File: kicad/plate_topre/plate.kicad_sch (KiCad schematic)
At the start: 72 parts, among them SW1 SW_Push, SW10 SW_Push, SW11 SW_Push, SW12 SW_Push, SW13 SW_Push, SW14 SW_Push, SW15 SW_Push, SW16 SW_Push, SW17 SW_Push, SW18 SW_Push, SW19 SW_Push, SW2 SW_Push, SW20 SW_Push, SW21 SW_Push, SW22 SW_Push, SW23 SW_Push, SW24 SW_Push, SW25 SW_Push, SW26 SW_Push, SW27 SW_Push, SW28 SW_Push, SW29 SW_Push, SW3 SW_Push, SW30 SW_Push, SW31 SW_Push, SW32 SW_Push, SW33 SW_Push, SW34 SW_Push, SW35 SW_Push, SW36 SW_Push, SW37 SW_Push, SW38 SW_Push, SW39 SW_Push, SW4 SW_Push, SW40 SW_Push, SW41 SW_Push, SW42 SW_Push, SW43 SW_Push, SW44 SW_Push, SW45 SW_Push, SW5 SW_Push, SW6 SW_Push, SW7 SW_Push, SW8 SW_Push, SW9 SW_Push

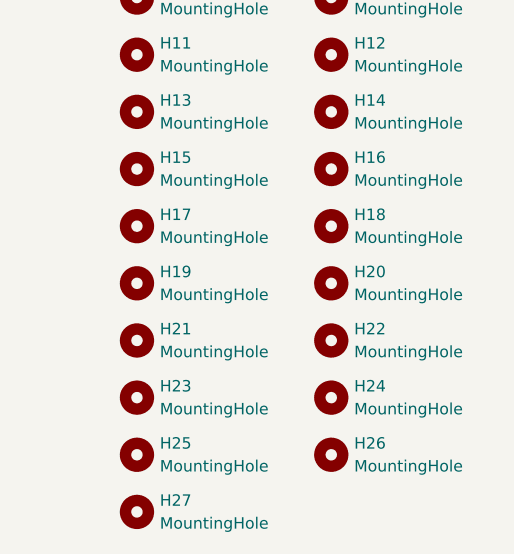
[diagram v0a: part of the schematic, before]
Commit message: updated footprint and fixing plate tolerance
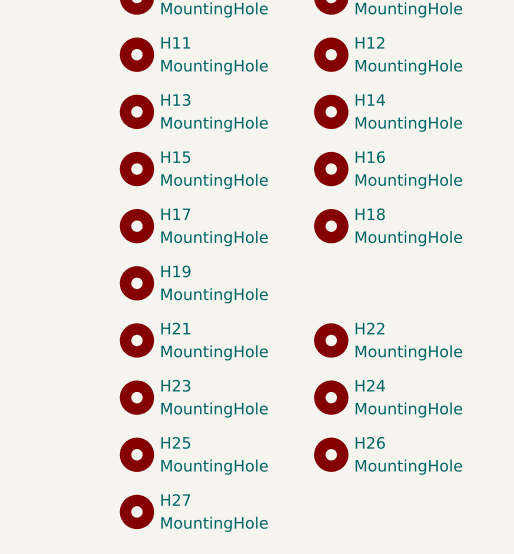
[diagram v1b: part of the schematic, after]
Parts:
- removed H20: MountingHole, MountingHole:MountingHole_3.2mm_M3_DIN965, symbol Mechanical:MountingHole
- H1, H10, H11, H12, H13, H14, H15, H16, H17, H18, H19, H2, H21, H22, H23, H24, H25, H26, H27, H3, H4, H5, H6, H7, H8, H9: footprint MountingHole:MountingHole_3.2mm_M3_DIN965 -> capacitive_sensors:MountingHole_2.2mm_M2
- SW1, SW10, SW11, SW12, SW13, SW15, SW16, SW17, SW18, SW19, SW2, SW20, SW21, SW22, SW23, SW24, SW25, SW27, SW28, SW29, SW3, SW30, SW31, SW32, SW33, SW34, SW35, SW36, SW37, SW4, SW5, SW6, SW7, SW8, SW9: footprint capacitive_sensors:ec_plate_cutout_topre_14.1x14.7mm -> capacitive_sensors:plate_cut_1U_topre
- SW14, SW39, SW44: footprint capacitive_sensors:ec_plate_cutout_topre_14.1x14.7mm -> capacitive_sensors:plate_cut_combo_0.25u_offset_topre
- SW26, SW41, SW42: footprint capacitive_sensors:ec_plate_cutout_topre_2u -> capacitive_sensors:plate_cut_2U_topre
- SW38, SW45: footprint capacitive_sensors:ec_plate_cutout_topre_14.1x14.7mm -> capacitive_sensors:plate_cut_combo_0.125u_offset_topre
- SW40, SW43: footprint capacitive_sensors:ec_plate_cutout_topre_14.1x14.7mm -> capacitive_sensors:plate_cut_combo_0.375u_offset_topre

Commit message: removing layout options for plates
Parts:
- SW38, SW45: footprint capacitive_sensors:plate_cut_combo_0.125u_offset_topre -> capacitive_sensors:plate_cut_1U_topre
- SW39, SW44: footprint capacitive_sensors:plate_cut_combo_0.25u_offset_topre -> capacitive_sensors:plate_cut_1U_topre
- SW40, SW43: footprint capacitive_sensors:plate_cut_combo_0.375u_offset_topre -> capacitive_sensors:plate_cut_1U_topre
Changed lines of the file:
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@@
       (effects (font (size 1.27 1.27)))
     )
-    (property "Footprint" "capacitive_sensors:plate_cut_combo_0.375u_offset_topre" (at 86.36 55.88 0)
+    (property "Footprint" "capacitive_sensors:plate_cut_1U_topre" (at 86.36 55.88 0)
       (effects (font (size 1.27 1.27)) hide)
     )
@@
       (effects (font (size 1.27 1.27)))
     )
-    (property "Footprint" "capacitive_sensors:plate_cut_combo_0.25u_offset_topre" (at 35.56 55.88 0)
+    (property "Footprint" "capacitive_sensors:plate_cut_1U_topre" (at 35.56 55.88 0)
       (effects (font (size 1.27 1.27)) hide)
     )
@@
       (effects (font (size 1.27 1.27)))
     )
-    (property "Footprint" "capacitive_sensors:plate_cut_combo_0.375u_offset_topre" (at 48.26 55.88 0)
+    (property "Footprint" "capacitive_sensors:plate_cut_1U_topre" (at 48.26 55.88 0)
       (effects (font (size 1.27 1.27)) hide)
     )
@@
       (effects (font (size 1.27 1.27)))
     )
-    (property "Footprint" "capacitive_sensors:plate_cut_combo_0.125u_offset_topre" (at 22.86 55.88 0)
+    (property "Footprint" "capacitive_sensors:plate_cut_1U_topre" (at 22.86 55.88 0)
       (effects (font (size 1.27 1.27)) hide)
     )
@@
       (effects (font (size 1.27 1.27)))
     )
-    (property "Footprint" "capacitive_sensors:plate_cut_combo_0.25u_offset_topre" (at 99.06 55.88 0)
+    (property "Footprint" "capacitive_sensors:plate_cut_1U_topre" (at 99.06 55.88 0)
       (effects (font (size 1.27 1.27)) hide)
     )
@@
       (effects (font (size 1.27 1.27)))
     )
-    (property "Footprint" "capacitive_sensors:plate_cut_combo_0.125u_offset_topre" (at 111.76 55.88 0)
-      (effects (font (size 1.27 1.27)) hide)
-    )
+    (property "Footprint" "capacitive_sensors:plate_cut_1U_topre" (at 111.76 55.88 0)
+      (effects (font (size 1.27 1.27)) hide)
+    )
